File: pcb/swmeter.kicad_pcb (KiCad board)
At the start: 2 copper layers, 100.1 x 100.2 mm, 26 parts, among them J1 BNC Conn_Coaxial, J2 3.5mm AudioPlug, J3_Meter1 Conn_01x02_Male, SW1 SW_DIP_x01, SW2 SW_DIP_x03, U1 LM3914N

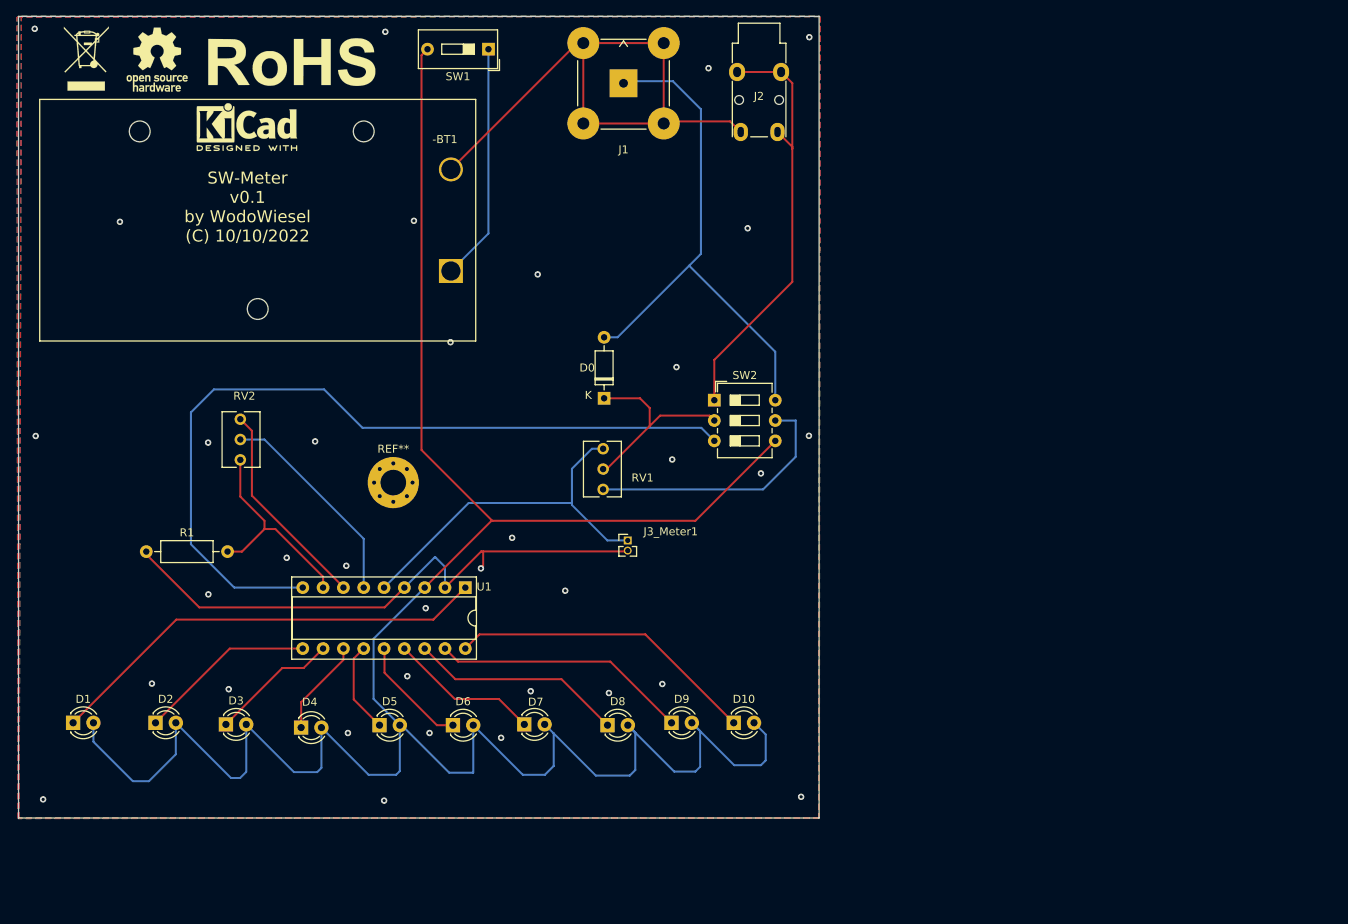
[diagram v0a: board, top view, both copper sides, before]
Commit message: design optimizations by adding input switch
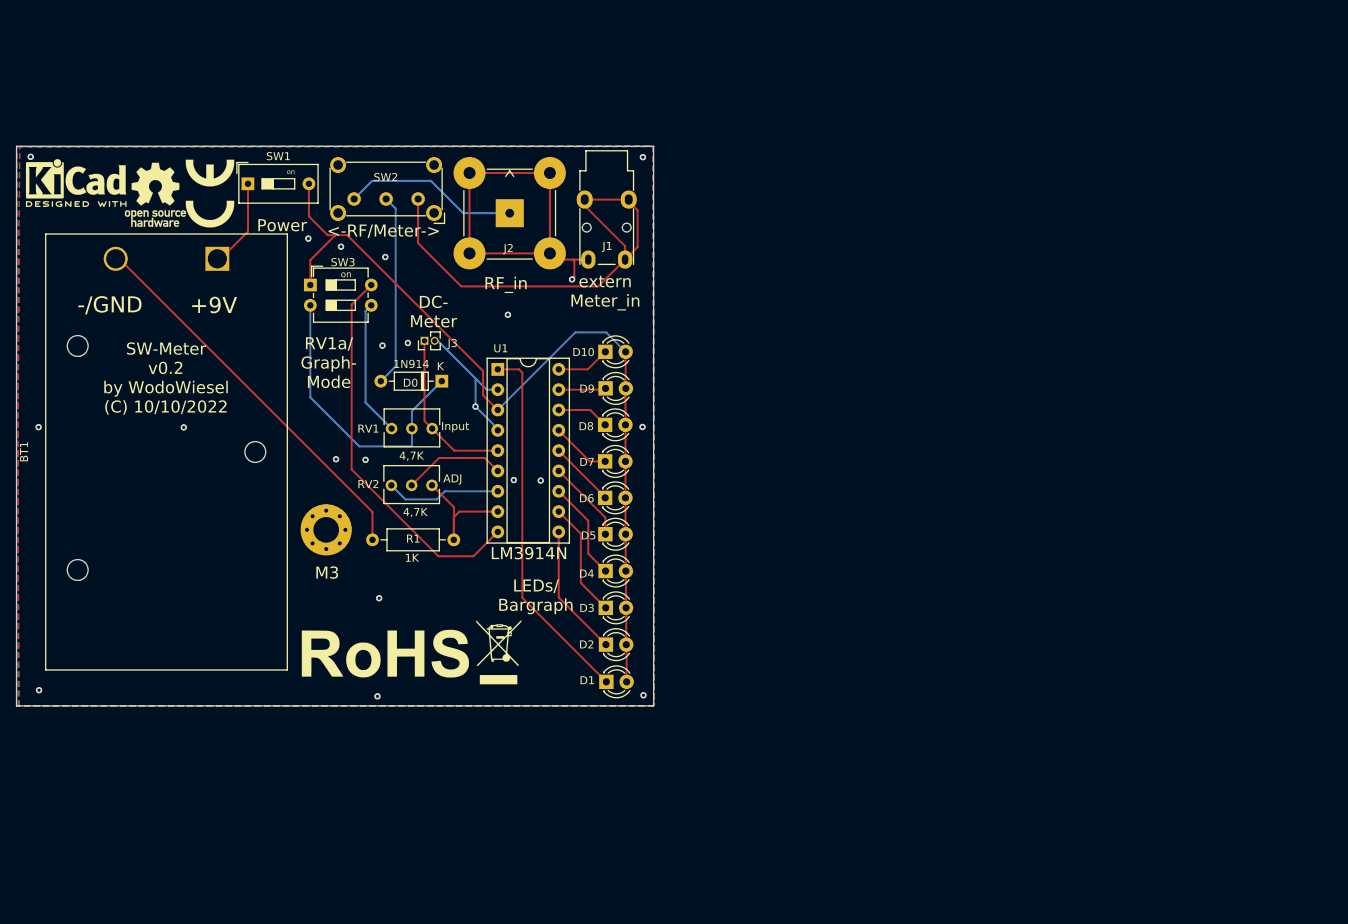
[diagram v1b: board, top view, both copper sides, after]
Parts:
- removed -BT1: Battery_Cell, Battery:BatteryHolder_Eagle_12BH611-GR
- added BT1: Battery_Cell, Battery:BatteryHolder_Eagle_12BH611-GR, F.Cu at (123.2, 69.3)
- added REF00: WEEE-Logo_5.6x8mm_SilkScreen, Symbol:WEEE-Logo_5.6x8mm_SilkScreen, B.Cu at (158.5, 118.5)
- added REF2: CE-Logo_8.5x6mm_SilkScreen, Symbol:CE-Logo_8.5x6mm_SilkScreen, B.Cu at (122.4, 60.8)
- added REF22: CE-Logo_8.5x6mm_SilkScreen, Symbol:CE-Logo_8.5x6mm_SilkScreen, F.Cu at (122.3, 61.1)
- added REF33: OSHW-Logo_7.5x8mm_SilkScreen, Symbol:OSHW-Logo_7.5x8mm_SilkScreen, B.Cu at (115.6, 61.1)
- added REF44: KiCad-Logo2_5mm_SilkScreen, Symbol:KiCad-Logo2_5mm_SilkScreen, B.Cu at (105.7, 59.9)
- added REF55: RoHS-Logo_6mm_SilkScreen, Symbol:RoHS-Logo_6mm_SilkScreen, B.Cu at (143.8, 118.7)
- added SW3: SW_DIP_x02, Button_Switch_THT:SW_DIP_SPSTx02_Slide_6.7x6.64mm_W7.62mm_P2.54mm_LowProfile, F.Cu at (134.9, 72.6)
- J1: value BNC Conn_Coaxial -> AudioPlug; footprint Connector_Coaxial:BNC_TEConnectivity_1478035_Horizontal -> Connector_Audio:Jack_3.5mm_Lumberg_1503_07_Horizontal
- J2: value 3.5mm AudioPlug -> Conn_Coaxial; footprint Connector_Audio:Jack_3.5mm_Lumberg_1503_07_Horizontal -> Connector_Coaxial:BNC_TEConnectivity_1478035_Horizontal
- SW2: value SW_DIP_x03 -> SW_SPDT; footprint Button_Switch_THT:SW_DIP_SPSTx03_Slide_6.7x9.18mm_W7.62mm_P2.54mm_LowProfile -> Button_Switch_THT:SW_E-Switch_EG1224_SPDT_Angled
- moved REF0 90.3 mm to (158.4, 118.5)
- moved REF5 74.9 mm to (144.3, 118.7)
- moved D1 66.9 mm to (171.9, 122.2)
- moved D2 57.1 mm to (171.8, 117.5)
- moved D3 49.7 mm to (171.8, 112.9)
- moved D10 49.1 mm to (171.8, 80.9)
- moved SW2 44.8 mm to (148.3, 61.8), turned to 180 degrees
- moved D4 42.8 mm to (171.8, 108.3)
- moved D9 42.6 mm to (171.8, 85.5)
- moved D8 37.5 mm to (171.7, 90.1)
- moved D5 37.0 mm to (171.8, 103.7)
- moved J3_Meter1 35.6 mm to (149.2, 79.5), turned to 90 degrees
- moved SW1 34.4 mm to (127.1, 59.9), turned to 0 degrees
- moved D7 34.4 mm to (171.7, 94.6)
- moved D6 34.2 mm to (171.7, 99.2)
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- renumbered REF** to REF0, REF** to REF1, REF** to REF3, REF** to REF4, REF** to REF5
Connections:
- SW2 pad 1: Net-(J2-PadR) -> Net-(J1-PadR)
- SW2 pad 2: Net-(D0-Pad1) -> Net-(D0-Pad2)
- SW2 pad 3: Net-(SW2-Pad3) -> Net-(J2-Pad1)
- U1 pad 9: Net-(SW2-Pad3) -> Net-(SW3-Pad4)
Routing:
- net Net-(D1-Pad2): track 298.4 -> 109.1 mm
- net Net-(SW2-Pad3): track 102.0 -> 0.00 mm
- net Net-(J1-PadR): track 0.00 -> 58.8 mm
- net Net-(J2-PadR): track 54.0 -> 0.00 mm
- net Net-(SW3-Pad4): track 0.00 -> 48.1 mm
- net Net-(D0-Pad2): track 67.0 -> 24.5 mm
- net GND: track 146.7 -> 114.5 mm, vias 35 -> 21
- net Net-(D10-Pad1): track 38.9 -> 6.73 mm
- net Net-(D9-Pad1): track 32.2 -> 5.91 mm
- net Net-(J3_Meter1-Pad1): track 46.2 -> 20.7 mm
- net Net-(J2-Pad1): track 0.00 -> 21.8 mm
- net Net-(D8-Pad1): track 26.8 -> 6.57 mm
- net +9V: track 29.7 -> 11.1 mm
- net Net-(RV1-Pad1): track 32.9 -> 17.1 mm
- net Net-(RV2-Pad2): track 26.7 -> 12.9 mm
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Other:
- board size 100.1 x 100.2 mm -> 79.6 x 70 mm
- board text added: "+9V"
- board text added: "-/GND"
- board text added: "1K"
- board text added: "1N914"
- board text added: "4,7K"
- board text added: "<-RF/Meter->"
- board text added: "ADJ"
- board text added: "Battery"
- board text added: "D0"
- board text added: "D1"
- board text added: "D10"
- board text added: "D2"
- board text added: "D3"
- board text added: "D4"
- board text added: "D5"
- board text added: "D6"
- board text added: "D7"
- board text added: "D8"
- board text added: "D9"
- board text added: "DC- Meter"
- board text added: "Input"
- board text added: "J1"
- board text added: "J2"
- board text added: "J3"
- board text added: "K"
- board text added: "LEDs/ Bargraph"
- board text added: "LM3914N"
- board text added: "M3"
- board text added: "Power"
- board text added: "R1"
- board text added: "RF_in"
- board text added: "RV1"
- board text added: "RV1a/ Graph- Mode"
- board text added: "RV2"
- board text added: "SW-Meter v0.2 by WodoWiesel (C) 10/10/2022"
- board text added: "SW2"
- board text added: "SW3"
- board text added: "U1"
- board text added: "extern Meter_in"
- board text removed: "SW-Meter v0.1 by WodoWiesel (C) 10/10/2022"

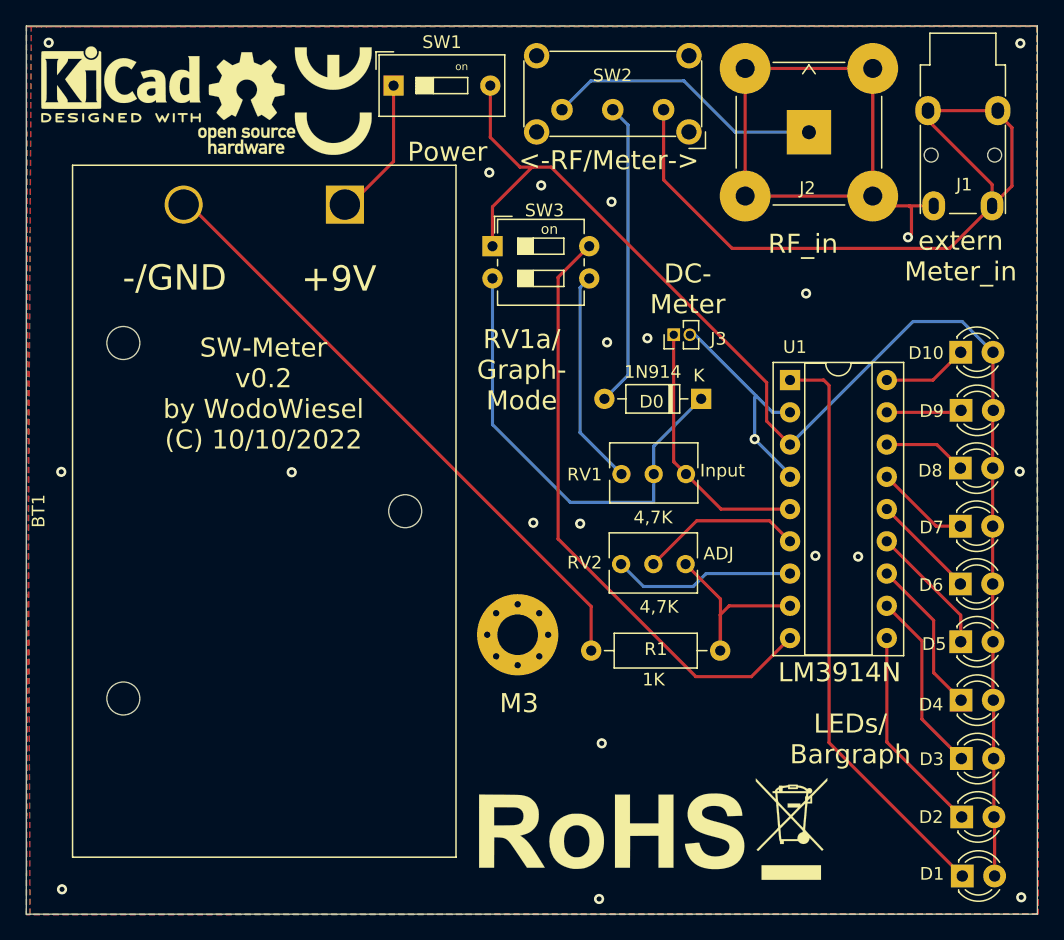
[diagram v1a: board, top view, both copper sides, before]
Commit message: Opimizations - prettify Silkscreens & Routings - DC-Meter 3-Pin Hheader - Gerber & Layer Files
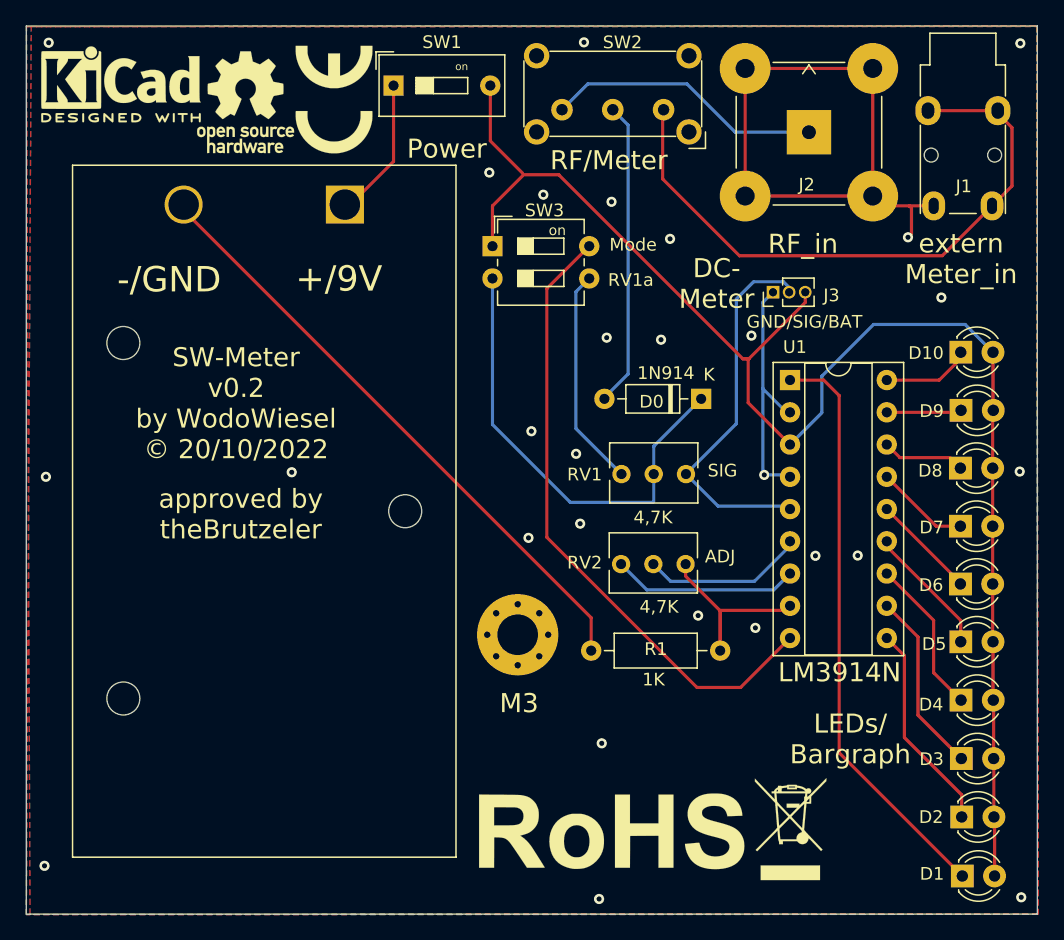
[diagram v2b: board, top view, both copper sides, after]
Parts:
- removed J3_Meter1: Conn_01x02_Male, Connector_PinHeader_1.27mm:PinHeader_1x02_P1.27mm_Vertical
- added J3: Conn_01x03_Female, Connector_PinHeader_1.27mm:PinHeader_1x03_P1.27mm_Vertical, F.Cu at (157.0, 76.2)
- moved REF22 0.13 mm to (122.4, 61.0)
- moved REF3 0.11 mm to (115.4, 61.2)
- moved REF0 0.08 mm to (158.3, 118.5)
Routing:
- net Net-(J3-Pad2): track 20.7 -> 30.1 mm
- net Net-(J1-PadR): track 58.8 -> 49.7 mm
- net Net-(D1-Pad2): track 109.1 -> 117.4 mm
- net Net-(SW3-Pad4): track 48.1 -> 50.0 mm
- net GND: track 114.5 -> 116.0 mm, vias 21 -> 28
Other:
- board text added: "+/9V"
- board text added: "GND/SIG/BAT"
- board text added: "Mode"
- board text added: "RF/Meter"
- board text added: "RV1a"
- board text added: "SIG"
- board text added: "SW-Meter v0.2 by WodoWiesel © 20/10/2022"
- board text added: "SW1"
- board text added: "approved by theBrutzeler"
- board text added: "on"
- board text removed: "+9V"
- board text removed: "<-RF/Meter->"
- board text removed: "Input"
- board text removed: "RV1a/ Graph- Mode"
- board text removed: "SW-Meter v0.2 by WodoWiesel (C) 10/10/2022"

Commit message: export update
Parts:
- removed REF2, REF22: CE-Logo_8.5x6mm_SilkScreen, Symbol:CE-Logo_8.5x6mm_SilkScreen
- added CV1: 22 µF, Capacitor_THT:CP_Radial_D5.0mm_P2.50mm, F.Cu at (161.3, 78.2)
- R1: value 1K -> 330Ω
- RV1: value R_Potentiometer_Trim -> 4,7 kΩ
- RV2: value 4,7K -> 4,7kΩ
- moved REF3 4.88 mm to (120.2, 60.5)
- moved REF33 4.76 mm to (120.3, 60.5)
- moved J3 4.01 mm to (153.0, 76.0)
- moved REF4 3.07 mm to (108.5, 60.7)
- moved REF44 2.95 mm to (108.5, 60.8)
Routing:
- net GND: track 116.0 -> 127.1 mm, vias 28 -> 30
- net Net-(J3-Pad2): track 30.1 -> 25.9 mm
- net Net-(CV1-Pad1): track 117.4 -> 119.7 mm
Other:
- board text added: "22 µF"
- board text added: "330Ω"
- board text added: "4,7kΩ"
- board text added: "CV1"
- board text added: "R<->Ext."
- board text added: "RF<->Ext."
- board text removed: "1K"
- board text removed: "4,7K"
- board text removed: "RF/Meter"

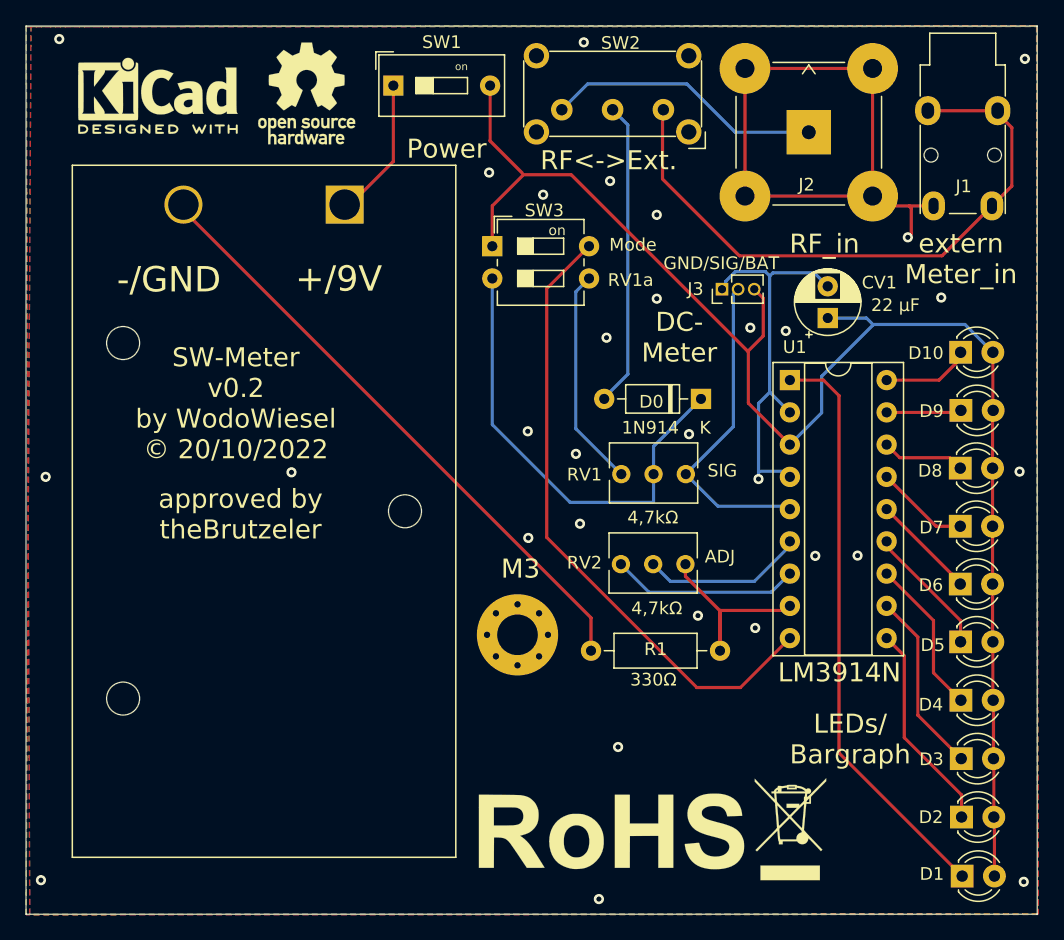
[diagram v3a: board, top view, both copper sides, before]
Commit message: -double trace width -use 2 same switches -add recycling logo -add HASL info -optimize gnd-plane
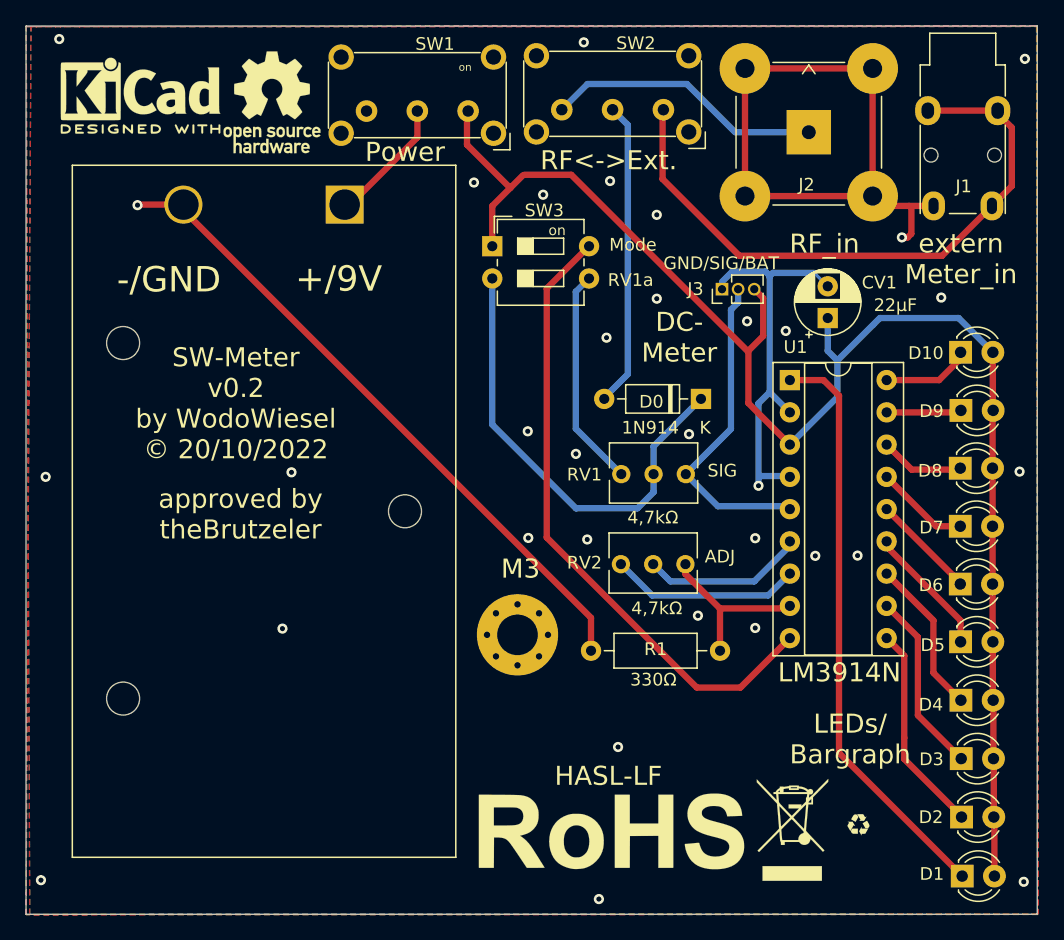
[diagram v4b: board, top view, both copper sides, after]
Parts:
- added G9: LOGO, Logos:recycling-symbol-kicad, F.Cu at (163.7, 118.1)
- added G99: LOGO, Logos:recycling-symbol-kicad, B.Cu at (163.8, 118.2)
- CV1: value 22 µF -> 22µF
- RV1: value 4,7 kΩ -> 4,7kΩ
- SW1: value SW_DIP_x01 -> SW_SPDT; footprint Button_Switch_THT:SW_DIP_SPSTx01_Slide_9.78x4.72mm_W7.62mm_P2.54mm -> Button_Switch_THT:SW_E-Switch_EG1224_SPDT_Angled
- moved SW1 6.22 mm to (133.0, 61.9), turned to 180 degrees
- moved REF33 2.83 mm to (117.6, 61.2)
- moved REF3 2.82 mm to (117.5, 61.2)
- moved REF4 1.37 mm to (107.2, 60.7)
- moved REF44 1.30 mm to (107.2, 60.8)
- moved REF0 0.17 mm to (158.5, 118.5)
- moved REF00 0.12 mm to (158.4, 118.6)
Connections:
- SW1 pad 1: +9V -> Net-(CV1-Pad1)
- SW1 pad 2: Net-(CV1-Pad1) -> +9V
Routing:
- net GND: track 127.1 -> 131.8 mm, vias 30 -> 33
- net +9V: track 11.1 -> 9.83 mm
- net Net-(D0-Pad2): track 24.5 -> 24.0 mm
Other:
- board text added: "HASL-LF"
